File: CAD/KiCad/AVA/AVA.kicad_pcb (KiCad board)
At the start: 2 copper layers, 100 x 75 mm, 44 parts, among them J1 Conn_01x03_Pin, J10 Conn_01x04_Pin, J2 Conn_01x03_Pin, J3 Conn_01x03_Pin, J4 Conn_01x03_Pin, J5 Conn_01x02_Pin, J6 Conn_01x02_Pin, J7 Conn_01x02_Pin, J8 Conn_01x03_Pin, J9 Conn_01x03_Pin, U1 WEMOS_C3_mini

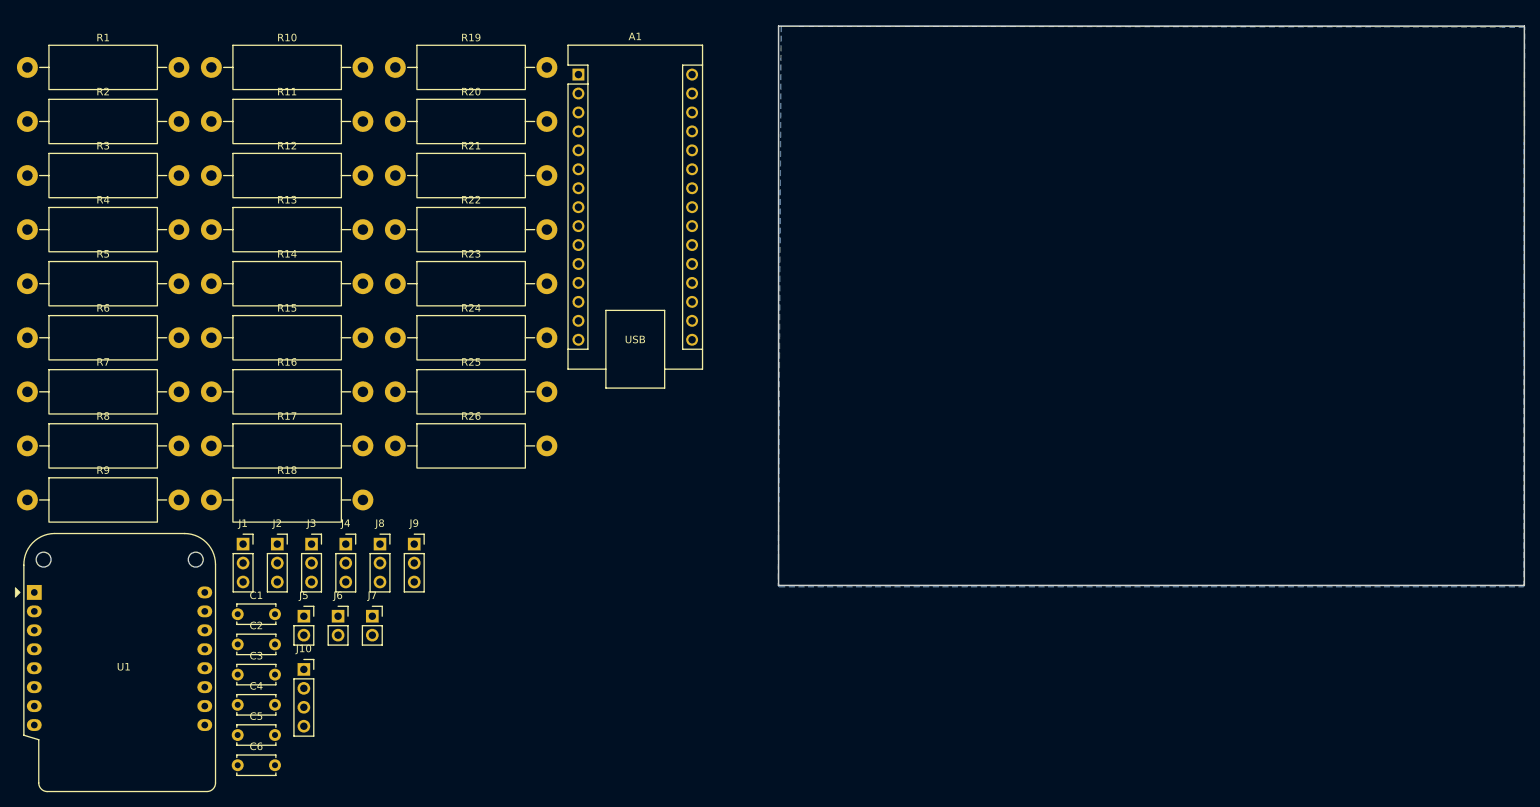
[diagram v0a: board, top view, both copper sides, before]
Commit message: Starting on tracks. PCB will be one-sided, billions must use wire bridges
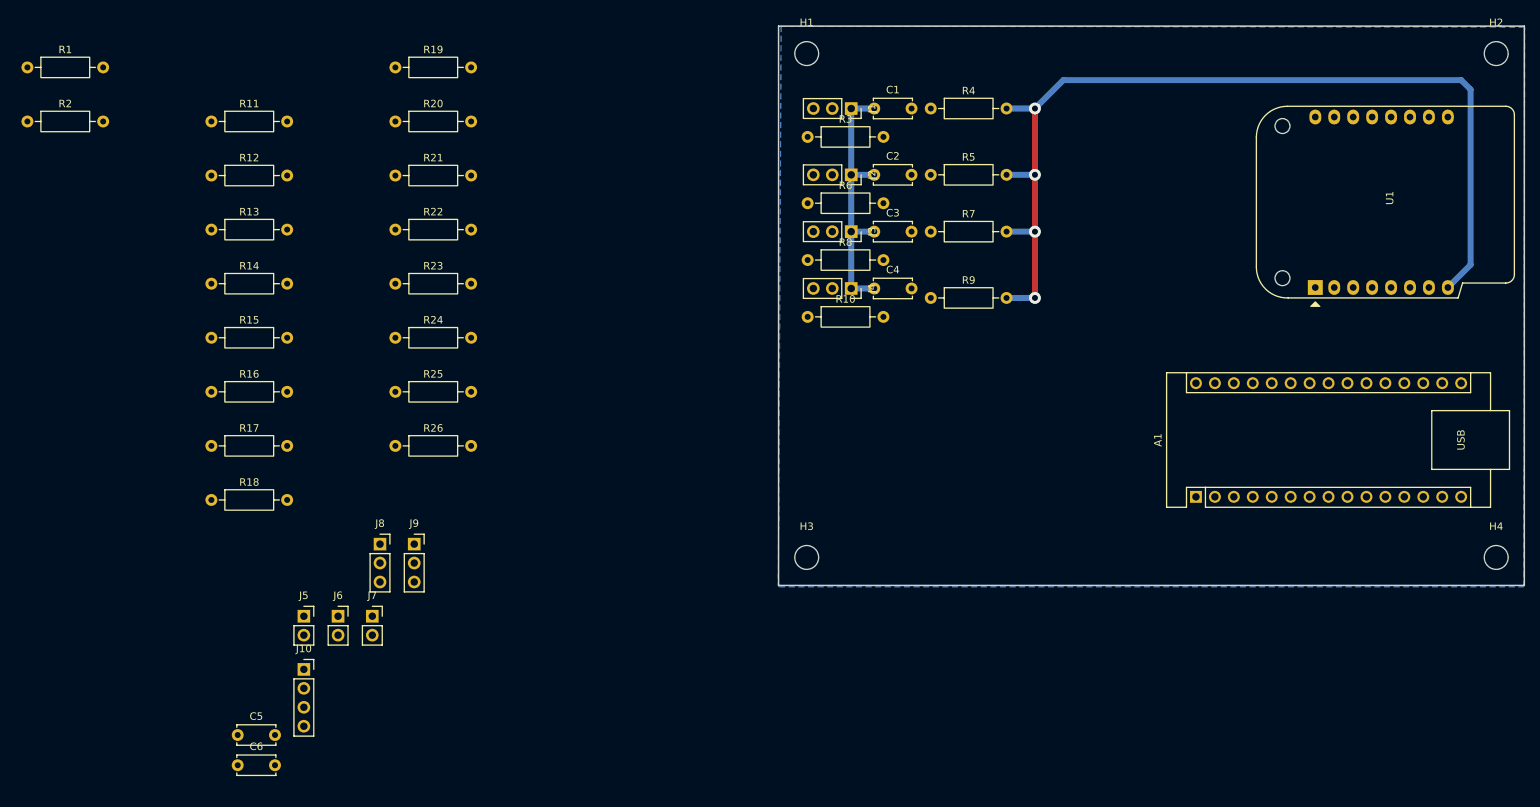
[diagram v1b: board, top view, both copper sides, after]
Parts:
- added H1: MountingHole, MountingHole:MountingHole_3.2mm_M3, F.Cu at (130.7, 54.9)
- added H2: MountingHole, MountingHole:MountingHole_3.2mm_M3, F.Cu at (223.1, 54.9)
- added H3: MountingHole, MountingHole:MountingHole_3.2mm_M3, F.Cu at (130.7, 122.4)
- added H4: MountingHole, MountingHole:MountingHole_3.2mm_M3, F.Cu at (223.1, 122.4)
- R1, R10, R11, R12, R13, R14, R15, R16, R17, R18, R19, R2, R20, R21, R22, R23, R24, R25, R26, R3, R4, R5, R6, R7, R8, R9: footprint Resistor_THT:R_Axial_DIN0614_L14.3mm_D5.7mm_P20.32mm_Horizontal -> Resistor_THT:R_Axial_DIN0207_L6.3mm_D2.5mm_P10.16mm_Horizontal
- moved U1 176.6 mm to (198.9, 86.2), turned to 90 degrees
- moved R9 124.1 mm to (147.3, 87.6)
- moved R7 123.0 mm to (147.3, 78.7)
- moved R4 122.2 mm to (147.3, 62.2)
- moved R5 122.0 mm to (147.3, 71.1)
- moved C1 109.0 mm to (139.7, 62.2)
- moved R8 107.6 mm to (130.8, 82.5)
- moved R6 106.2 mm to (130.8, 74.9)
- moved C2 106.1 mm to (139.7, 71.1)
- moved R3 104.8 mm to (130.8, 66.0)
- moved C3 104.0 mm to (139.7, 78.7)
- moved C4 102.0 mm to (139.7, 86.4)
- moved A1 100.3 mm to (182.9, 114.3), turned to 90 degrees
- moved J1 100.3 mm to (136.7, 62.2), turned to -90 degrees
- moved J2 91.5 mm to (136.7, 71.1), turned to -90 degrees
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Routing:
- net Net-(U1-3V3): track 0.00 -> 129.0 mm, vias 0 -> 4
- net Net-(J1-Pin_1): track 0.00 -> 36.5 mm

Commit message: Need to figure out how to hotkey batch track deletion. Need more autism, administering  0.5cc of Covid-19 vaccine for enhanced performance
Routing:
- net Net-(U1-3V3): track 129.0 -> 0.00 mm, vias 4 -> 0
- net Net-(J1-Pin_1): track 36.5 -> 0.00 mm
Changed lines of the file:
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@@
 		(layer "Edge.Cuts")
-	)
-	(segment
-		(start 136.652 78.74)
-		(end 136.652 86.36)
-		(width 0.8)
-		(layer "B.Cu")
-		(net "Net-(J1-Pin_1)")
-	)
-	(segment
-		(start 139.74 78.74)
-		(end 136.652 78.74)
-		(width 0.8)
-		(layer "B.Cu")
-		(net "Net-(J1-Pin_1)")
-	)
-	(segment
-		(start 136.652 62.23)
-		(end 136.652 71.12)
-		(width 0.8)
-		(layer "B.Cu")
-		(net "Net-(J1-Pin_1)")
-	)
-	(segment
-		(start 139.74 86.36)
-		(end 136.652 86.36)
-		(width 0.8)
-		(layer "B.Cu")
-		(net "Net-(J1-Pin_1)")
-	)
-	(segment
-		(start 139.74 71.12)
-		(end 136.652 71.12)
-		(width 0.8)
-		(layer "B.Cu")
-		(net "Net-(J1-Pin_1)")
-	)
-	(segment
-		(start 136.652 71.12)
-		(end 136.652 78.74)
-		(width 0.8)
-		(layer "B.Cu")
-		(net "Net-(J1-Pin_1)")
-	)
-	(segment
-		(start 139.74 62.23)
-		(end 136.652 62.23)
-		(width 0.8)
-		(layer "B.Cu")
-		(net "Net-(J1-Pin_1)")
-	)
-	(segment
-		(start 161.29 78.74)
-		(end 161.29 87.63)
-		(width 0.8)
-		(layer "F.Cu")
-		(net "Net-(U1-3V3)")
-	)
-	(segment
-		(start 161.29 71.12)
-		(end 161.29 78.74)
-		(width 0.8)
-		(layer "F.Cu")
-		(net "Net-(U1-3V3)")
-	)
-	(segment
-		(start 161.29 62.23)
-		(end 161.29 71.12)
-		(width 0.8)
-		(layer "F.Cu")
-		(net "Net-(U1-3V3)")
-	)
-	(via
-		(at 161.29 87.63)
-		(size 1.6)
-		(drill 0.8)
-		(layers "F.Cu" "B.Cu")
-		(net "Net-(U1-3V3)")
-	)
-	(via
-		(at 161.29 62.23)
-		(size 1.6)
-		(drill 0.8)
-		(layers "F.Cu" "B.Cu")
-		(net "Net-(U1-3V3)")
-	)
-	(via
-		(at 161.29 71.12)
-		(size 1.6)
-		(drill 0.8)
-		(layers "F.Cu" "B.Cu")
-		(net "Net-(U1-3V3)")
-	)
-	(via
-		(at 161.29 78.74)
-		(size 1.6)
-		(drill 0.8)
-		(layers "F.Cu" "B.Cu")
-		(net "Net-(U1-3V3)")
-	)
-	(segment
-		(start 218.44 58.42)
-		(end 219.71 59.69)
-		(width 0.8)
-		(layer "B.Cu")
-		(net "Net-(U1-3V3)")
-	)
-	(segment
-		(start 157.48 87.63)
-		(end 161.29 87.63)
-		(width 0.8)
-		(layer "B.Cu")
-		(net "Net-(U1-3V3)")
-	)
-	(segment
-		(start 157.48 71.12)
-		(end 161.29 71.12)
-		(width 0.8)
-		(layer "B.Cu")
-		(net "Net-(U1-3V3)")
-	)
-	(segment
-		(start 157.48 62.23)
-		(end 161.29 62.23)
-		(width 0.8)
-		(layer "B.Cu")
-		(net "Net-(U1-3V3)")
-	)
-	(segment
-		(start 219.71 83.18)
-		(end 216.66 86.23)
-		(width 0.8)
-		(layer "B.Cu")
-		(net "Net-(U1-3V3)")
-	)
-	(segment
-		(start 157.48 78.74)
-		(end 161.29 78.74)
-		(width 0.8)
-		(layer "B.Cu")
-		(net "Net-(U1-3V3)")
-	)
-	(segment
-		(start 165.1 58.42)
-		(end 218.44 58.42)
-		(width 0.8)
-		(layer "B.Cu")
-		(net "Net-(U1-3V3)")
-	)
-	(segment
-		(start 161.29 62.23)
-		(end 165.1 58.42)
-		(width 0.8)
-		(layer "B.Cu")
-		(net "Net-(U1-3V3)")
-	)
-	(segment
-		(start 219.71 59.69)
-		(end 219.71 83.18)
-		(width 0.8)
-		(layer "B.Cu")
-		(net "Net-(U1-3V3)")
 	)
 	(zone
